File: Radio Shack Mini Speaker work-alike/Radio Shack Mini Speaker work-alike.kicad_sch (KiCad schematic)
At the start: 22 parts, among them J1 SJ1-3525N, J2 SJ1-3525N, Q1 2SC1815, SW1 SW_SPDT, U1 LM386

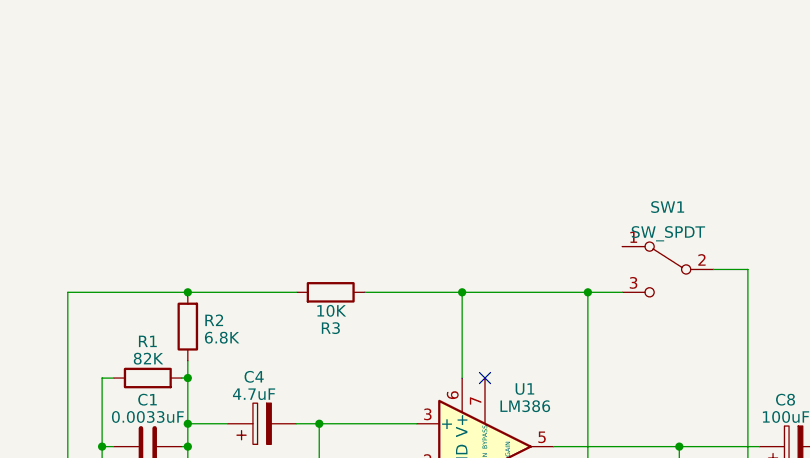
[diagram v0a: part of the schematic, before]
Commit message: added power led
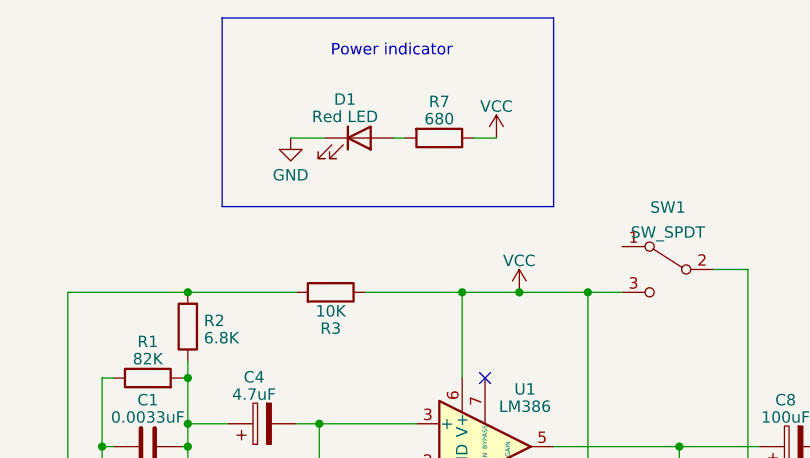
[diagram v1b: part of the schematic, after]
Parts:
- added D1: Red LED, symbol Device:LED
- added R7: 680, symbol Device:R
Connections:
- net GND: now also D1.1 (K)
- net VCC: now reaches C7.1, R3.1, SW1.3 (C), U1.6 (V+)
- net VCC: now also R7.1
- new net: D1.2 (A), R7.2
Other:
- note added: "Power indicator"
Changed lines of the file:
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@@
   (junction (at 125.095 80.645) (diameter 0) (color 0 0 0 0)
+  )
+  (junction (at 131.445 80.645) (diameter 0) (color 0 0 0 0)
   )
   (junction (at 109.22 95.25) (diameter 0) (color 0 0 0 0)
@@
     (stroke (width 0) (type default))
   )
+  (wire (pts (xy 126.365 63.5) (xy 128.905 63.5))
+    (stroke (width 0) (type default))
+  )
   (wire (pts (xy 139.065 80.645) (xy 139.065 109.22))
     (stroke (width 0) (type default))
@@
     (stroke (width 0) (type default))
   )
-  (wire (pts (xy 125.095 80.645) (xy 139.065 80.645))
+  (wire (pts (xy 125.095 80.645) (xy 131.445 80.645))
     (stroke (width 0) (type default))
   )
@@
     (stroke (width 0) (type default))
   )
+  (wire (pts (xy 106.045 63.5) (xy 109.855 63.5))
+    (stroke (width 0) (type default))
+  )
   (wire (pts (xy 109.22 124.46) (xy 109.22 121.92))
     (stroke (width 0) (type default))
@@
     (stroke (width 0) (type default))
   )
+  (wire (pts (xy 131.445 80.645) (xy 139.065 80.645))
+    (stroke (width 0) (type default))
+  )
   (wire (pts (xy 149.225 113.665) (xy 149.225 108.585))
     (stroke (width 0) (type default))
@@
     (stroke (width 0) (type default))
   )
+  (wire (pts (xy 117.475 63.5) (xy 118.745 63.5))
+    (stroke (width 0) (type default))
+  )
   (wire (pts (xy 174.625 113.665) (xy 169.545 113.665))
     (stroke (width 0) (type default))
@@
   (wire (pts (xy 85.09 106.045) (xy 86.995 106.045))
     (stroke (width 0) (type default))
+  )
+  (rectangle (start 98.425 50.165) (end 135.255 71.12)
+    (stroke (width 0) (type default))
+    (fill (type none))
+  )
+  (text "Power indicator" (at 110.49 54.61 0)
+    (effects (font (size 1.27 1.27)) (justify left bottom))
   )
   (symbol (lib_id "Device:C_Polarized") (at 131.445 111.76 90) (unit 1)
@@
     )
   )
+  (symbol (lib_id "power:VCC") (at 131.445 80.645 0) (unit 1)
+    (in_bom yes) (on_board yes) (dnp no) (fields_autoplaced)
+    (property "Reference" "#PWR01" (at 131.445 84.455 0)
+      (effects (font (size 1.27 1.27)) hide)
+    )
+    (property "Value" "VCC" (at 131.445 77.1431 0)
+      (effects (font (size 1.27 1.27)))
+    )
+    (property "Footprint" "" (at 131.445 80.645 0)
+      (effects (font (size 1.27 1.27)) hide)
+    )
+    (property "Datasheet" "" (at 131.445 80.645 0)
+      (effects (font (size 1.27 1.27)) hide)
+    )
+    (pin "1")
+    (instances
+      (project "Radio Shack Mini Speaker work-alike"
+        (path "/107d545c-a928-4c25-a52f-96fe59686438"
+          (reference "#PWR01") (unit 1)
+        )
+      )
+    )
+  )
   (symbol (lib_id "Evan's misc parts:SJ1-3525N") (at 41.91 102.87 0) (mirror x) (unit 1)
     (in_bom yes) (on_board yes) (dnp no) (fields_autoplaced)
@@
     )
   )
+  (symbol (lib_id "power:VCC") (at 128.905 63.5 0) (unit 1)
+    (in_bom yes) (on_board yes) (dnp no) (fields_autoplaced)
+    (property "Reference" "#PWR04" (at 128.905 67.31 0)
+      (effects (font (size 1.27 1.27)) hide)
+    )
+    (property "Value" "VCC" (at 128.905 59.9981 0)
+      (effects (font (size 1.27 1.27)))
+    )
+    (property "Footprint" "" (at 128.905 63.5 0)
+      (effects (font (size 1.27 1.27)) hide)
+    )
+    (property "Datasheet" "" (at 128.905 63.5 0)
+      (effects (font (size 1.27 1.27)) hide)
+    )
+    (pin "1")
+    (instances
+      (project "Radio Shack Mini Speaker work-alike"
+        (path "/107d545c-a928-4c25-a52f-96fe59686438"
+          (reference "#PWR04") (unit 1)
+        )
+      )
+    )
+  )
+  (symbol (lib_id "Device:LED") (at 113.665 63.5 0) (unit 1)
+    (in_bom yes) (on_board yes) (dnp no) (fields_autoplaced)
+    (property "Reference" "D1" (at 112.0775 59.2201 0)
+      (effects (font (size 1.27 1.27)))
+    )
+    (property "Value" "Red LED" (at 112.0775 61.1411 0)
+      (effects (font (size 1.27 1.27)))
+    )
+    (property "Footprint" "" (at 113.665 63.5 0)
+      (effects (font (size 1.27 1.27)) hide)
+    )
+    (property "Datasheet" "~" (at 113.665 63.5 0)
+      (effects (font (size 1.27 1.27)) hide)
+    )
+    (pin "1")
+    (pin "2")
+    (instances
+      (project "Radio Shack Mini Speaker work-alike"
+        (path "/107d545c-a928-4c25-a52f-96fe59686438"
+          (reference "D1") (unit 1)
+        )
+      )
+    )
+  )
   (symbol (lib_id "Device:R_Potentiometer") (at 67.31 106.045 0) (unit 1)
     (in_bom yes) (on_board yes) (dnp no) (fields_autoplaced)
@@
         )
       )
+    )
+  )
+  (symbol (lib_id "Device:R") (at 122.555 63.5 270) (unit 1)
+    (in_bom yes) (on_board yes) (dnp no)
+    (property "Reference" "R7" (at 122.555 59.4741 90)
+      (effects (font (size 1.27 1.27)))
+    )
+    (property "Value" "680" (at 122.555 61.3951 90)
+      (effects (font (size 1.27 1.27)))
+    )
+    (property "Footprint" "" (at 122.555 61.722 90)
+      (effects (font (size 1.27 1.27)) hide)
+    )
+    (property "Datasheet" "~" (at 122.555 63.5 0)
+      (effects (font (size 1.27 1.27)) hide)
+    )
+    (pin "1")
+    (pin "2")
+    (instances
+      (project "Radio Shack Mini Speaker work-alike"
+        (path "/107d545c-a928-4c25-a52f-96fe59686438"
+          (reference "R7") (unit 1)
+        )
+      )
+    )
+  )
+  (symbol (lib_id "power:GND") (at 106.045 63.5 0) (unit 1)
+    (in_bom yes) (on_board yes) (dnp no) (fields_autoplaced)
+    (property "Reference" "#PWR02" (at 106.045 69.85 0)
+      (effects (font (size 1.27 1.27)) hide)
+    )
+    (property "Value" "GND" (at 106.045 67.6355 0)
+      (effects (font (size 1.27 1.27)))
+    )
+    (property "Footprint" "" (at 106.045 63.5 0)
+      (effects (font (size 1.27 1.27)) hide)
+    )
+    (property "Datasheet" "" (at 106.045 63.5 0)
+      (effects (font (size 1.27 1.27)) hide)
+    )
+    (pin "1")
+    (instances
+      (project "Radio Shack Mini Speaker work-alike"
+        (path "/107d545c-a928-4c25-a52f-96fe59686438"
+          (reference "#PWR02") (unit 1)
+        )
+      )

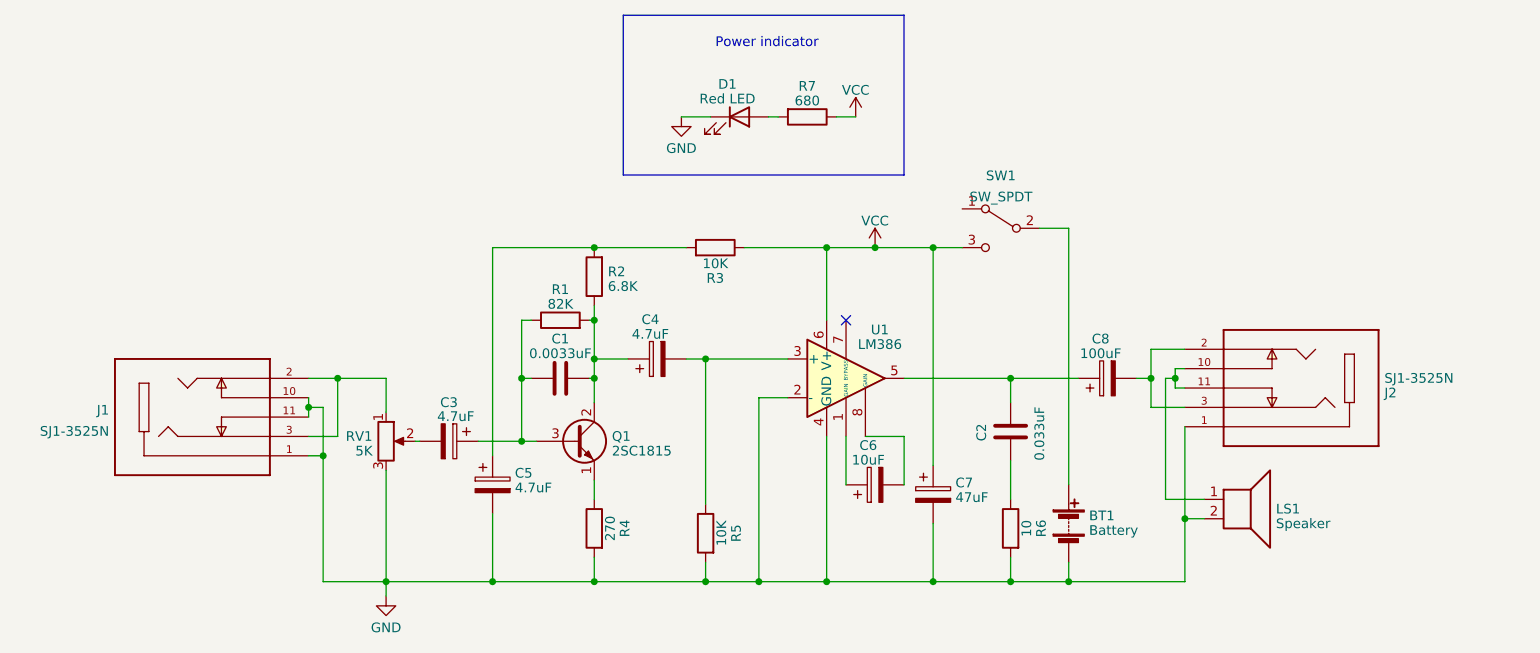
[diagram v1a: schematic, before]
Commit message: tweaked radio shack speaker
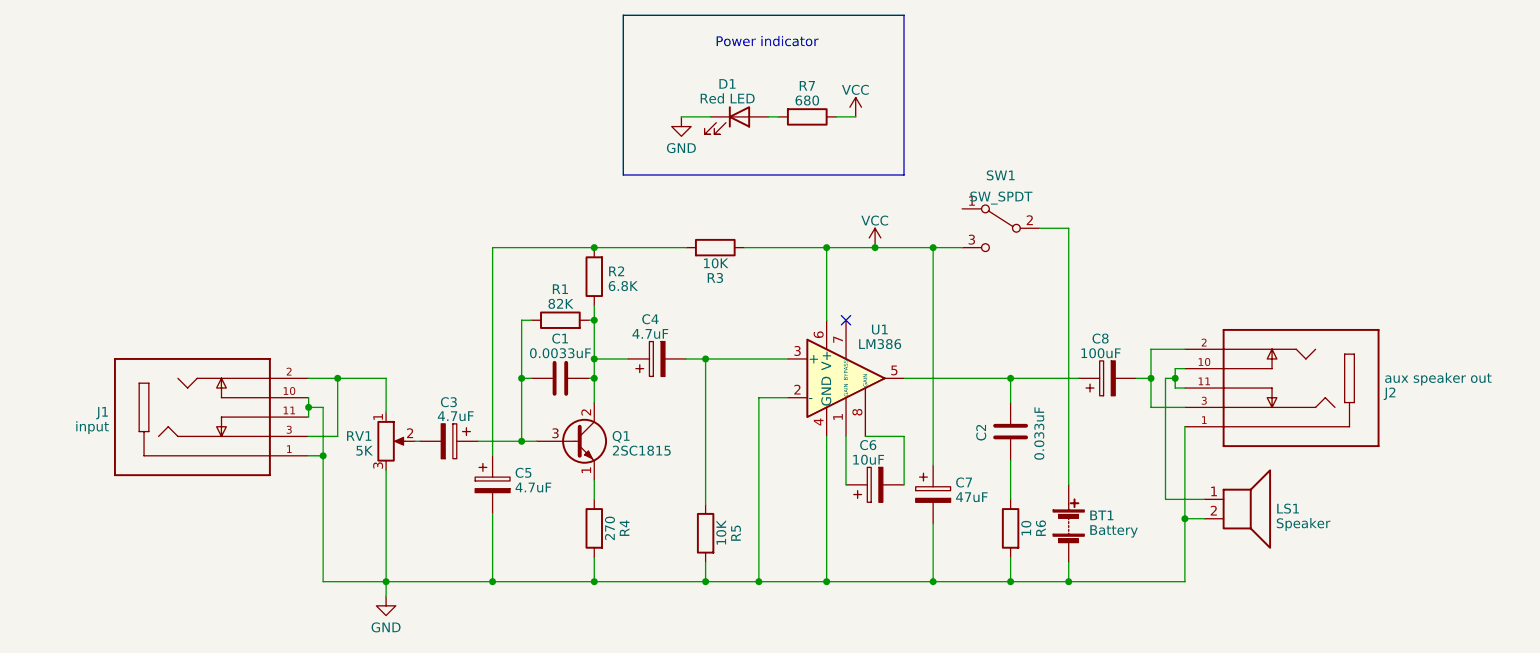
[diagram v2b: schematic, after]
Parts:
- BT1, LS1: footprint (none) -> Connector_PinHeader_2.54mm:PinHeader_1x02_P2.54mm_Vertical
- C6: footprint (none) -> Capacitor_THT:CP_Radial_D5.0mm_P2.50mm
- D1: footprint (none) -> LED_THT:LED_D3.0mm
- J1: value SJ1-3525N -> input; footprint Evan's misc parts:CUI_SJ1-3525N -> Evan's parts:CUI_SJ1-3525N
- J2: value SJ1-3525N -> aux speaker out; footprint Evan's misc parts:CUI_SJ1-3525N -> Evan's parts:CUI_SJ1-3525N
- R1, R2, R3, R4, R5, R6, R7: footprint (none) -> Resistor_THT:R_Axial_DIN0207_L6.3mm_D2.5mm_P10.16mm_Horizontal
- U1: footprint (none) -> Package_DIP:DIP-8_W7.62mm
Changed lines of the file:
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@@
       (effects (font (size 1.27 1.27)))
     )
-    (property "Footprint" "" (at 135.255 110.7948 0)
+    (property "Footprint" "Capacitor_THT:CP_Radial_D5.0mm_P2.50mm" (at 135.255 110.7948 0)
       (effects (font (size 1.27 1.27)) hide)
     )
@@
       (effects (font (size 1.27 1.27)))
     )
-    (property "Footprint" "" (at 151.003 117.475 90)
+    (property "Footprint" "Resistor_THT:R_Axial_DIN0207_L6.3mm_D2.5mm_P10.16mm_Horizontal" (at 151.003 117.475 90)
       (effects (font (size 1.27 1.27)) hide)
     )
@@
       (effects (font (size 1.27 1.27)))
     )
-    (property "Footprint" "" (at 96.393 117.475 90)
+    (property "Footprint" "Resistor_THT:R_Axial_DIN0207_L6.3mm_D2.5mm_P10.16mm_Horizontal" (at 96.393 117.475 90)
       (effects (font (size 1.27 1.27)) hide)
     )
@@
   (symbol (lib_id "Evan's misc parts:SJ1-3525N") (at 41.91 102.87 0) (mirror x) (unit 1)
     (in_bom yes) (on_board yes) (dnp no) (fields_autoplaced)
-    (property "Reference" "J1" (at 30.988 101.9615 0)
-      (effects (font (size 1.27 1.27)) (justify right))
-    )
-    (property "Value" "SJ1-3525N" (at 30.988 104.7366 0)
-      (effects (font (size 1.27 1.27)) (justify right))
-    )
-    (property "Footprint" "Evan's misc parts:CUI_SJ1-3525N" (at 41.91 102.87 0)
+    (property "Reference" "J1" (at 30.9881 102.2263 0)
+      (effects (font (size 1.27 1.27)) (justify right))
+    )
+    (property "Value" "input" (at 30.9881 104.1473 0)
+      (effects (font (size 1.27 1.27)) (justify right))
+    )
+    (property "Footprint" "Evan's parts:CUI_SJ1-3525N" (at 41.91 102.87 0)
       (effects (font (size 1.27 1.27)) (justify left bottom) hide)
     )
@@
       (effects (font (size 1.27 1.27)))
     )
-    (property "Footprint" "" (at 113.665 63.5 0)
+    (property "Footprint" "LED_THT:LED_D3.0mm" (at 113.665 63.5 0)
       (effects (font (size 1.27 1.27)) hide)
     )
@@
       (effects (font (size 1.27 1.27)) (justify left))
     )
-    (property "Footprint" "" (at 179.705 118.745 0)
+    (property "Footprint" "Connector_PinHeader_2.54mm:PinHeader_1x02_P2.54mm_Vertical" (at 179.705 118.745 0)
       (effects (font (size 1.27 1.27)) hide)
     )
@@
       (effects (font (size 1.27 1.27)) (justify right))
     )
-    (property "Footprint" "" (at 96.393 84.455 90)
+    (property "Footprint" "Resistor_THT:R_Axial_DIN0207_L6.3mm_D2.5mm_P10.16mm_Horizontal" (at 96.393 84.455 90)
       (effects (font (size 1.27 1.27)) hide)
     )
@@
       (effects (font (size 1.27 1.27)) (justify left))
     )
-    (property "Footprint" "" (at 156.845 115.316 90)
+    (property "Footprint" "Connector_PinHeader_2.54mm:PinHeader_1x02_P2.54mm_Vertical" (at 156.845 115.316 90)
       (effects (font (size 1.27 1.27)) hide)
     )
@@
       (effects (font (size 1.27 1.27)))
     )
-    (property "Footprint" "" (at 122.555 61.722 90)
+    (property "Footprint" "Resistor_THT:R_Axial_DIN0207_L6.3mm_D2.5mm_P10.16mm_Horizontal" (at 122.555 61.722 90)
       (effects (font (size 1.27 1.27)) hide)
     )
@@
       (effects (font (size 1.27 1.27)))
     )
-    (property "Footprint" "" (at 130.175 95.25 0)
+    (property "Footprint" "Package_DIP:DIP-8_W7.62mm" (at 130.175 95.25 0)
       (effects (font (size 1.27 1.27)) hide)
     )
@@
       (effects (font (size 1.27 1.27)))
     )
-    (property "Footprint" "" (at 110.49 82.423 90)
+    (property "Footprint" "Resistor_THT:R_Axial_DIN0207_L6.3mm_D2.5mm_P10.16mm_Horizontal" (at 110.49 82.423 90)
       (effects (font (size 1.27 1.27)) hide)
     )
@@
       (effects (font (size 1.27 1.27)) (justify right))
     )
-    (property "Value" "SJ1-3525N" (at 198.247 97.7827 0)
-      (effects (font (size 1.27 1.27)) (justify right))
-    )
-    (property "Footprint" "Evan's misc parts:CUI_SJ1-3525N" (at 187.325 99.06 0)
+    (property "Value" "aux speaker out" (at 198.247 97.7827 0)
+      (effects (font (size 1.27 1.27)) (justify right))
+    )
+    (property "Footprint" "Evan's parts:CUI_SJ1-3525N" (at 187.325 99.06 0)
       (effects (font (size 1.27 1.27)) (justify left bottom) hide)
     )
@@
       (effects (font (size 1.27 1.27)))
     )
-    (property "Footprint" "" (at 110.998 118.11 90)
+    (property "Footprint" "Resistor_THT:R_Axial_DIN0207_L6.3mm_D2.5mm_P10.16mm_Horizontal" (at 110.998 118.11 90)
       (effects (font (size 1.27 1.27)) hide)
     )
@@
       (effects (font (size 1.27 1.27)))
     )
-    (property "Footprint" "" (at 90.17 91.948 90)
-      (effects (font (size 1.27 1.27)) hide)
-    )
+    (property "Footprint" "Resistor_THT:R_Axial_DIN0207_L6.3mm_D2.5mm_P10.16mm_Horizontal" (at 90.17 91.948 90)
+      (effects (font (size 1.27 1.27)) hide)
+    )

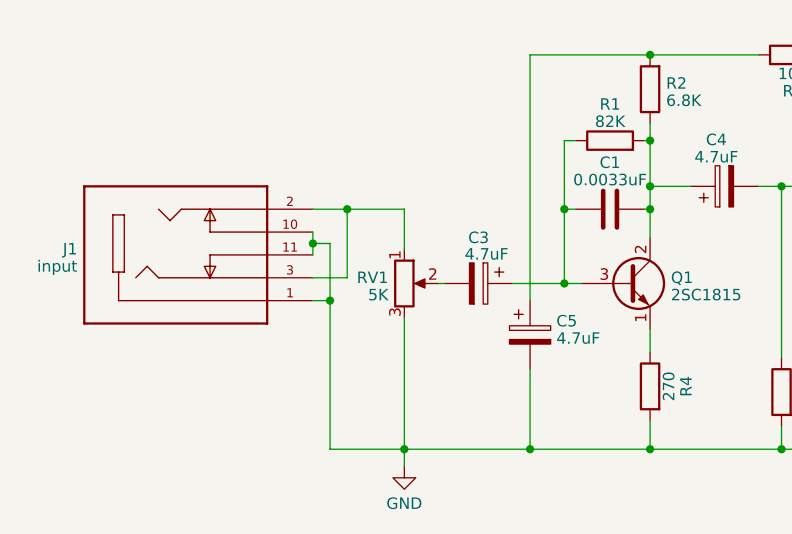
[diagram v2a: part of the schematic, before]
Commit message: updated switch position
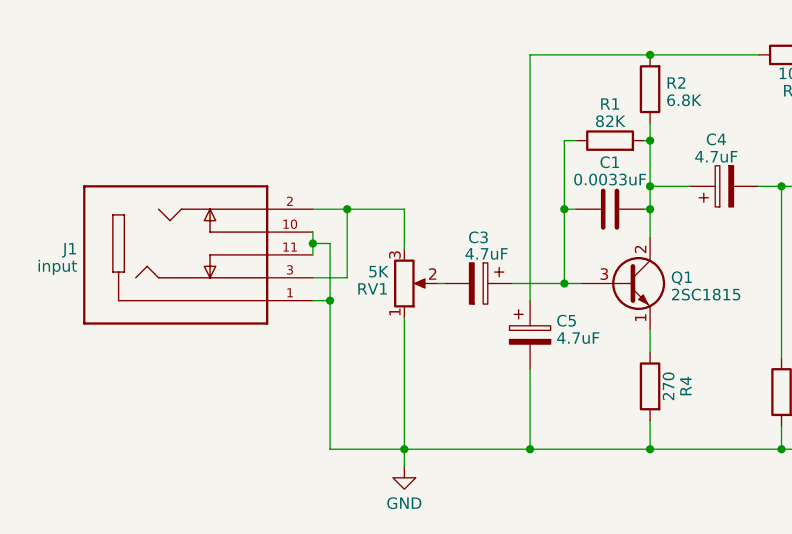
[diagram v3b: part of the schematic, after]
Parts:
- C1: footprint (none) -> Capacitor_THT:C_Disc_D5.0mm_W2.5mm_P2.50mm
- C2: footprint (none) -> Capacitor_THT:C_Disc_D5.0mm_W2.5mm_P5.00mm
- C3, C4, C5, C7: footprint (none) -> Capacitor_THT:CP_Radial_D5.0mm_P2.50mm
- C8: footprint (none) -> Capacitor_THT:CP_Radial_D6.3mm_P2.50mm
- RV1: footprint (none) -> Evan's parts:allen bradlet thumbwheel pot
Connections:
- net GND: now also RV1.1; no longer RV1.3
- net at J1.2, J1.3: now also RV1.3; no longer RV1.1
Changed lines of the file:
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@@
       (effects (font (size 1.27 1.27)) (justify left))
     )
-    (property "Footprint" "" (at 82.2452 115.57 0)
+    (property "Footprint" "Capacitor_THT:CP_Radial_D5.0mm_P2.50mm" (at 82.2452 115.57 0)
       (effects (font (size 1.27 1.27)) hide)
     )
@@
     )
   )
-  (symbol (lib_id "Device:R_Potentiometer") (at 67.31 106.045 0) (unit 1)
-    (in_bom yes) (on_board yes) (dnp no) (fields_autoplaced)
-    (property "Reference" "RV1" (at 65.5321 105.4013 0)
-      (effects (font (size 1.27 1.27)) (justify right))
-    )
-    (property "Value" "5K" (at 65.5321 107.3223 0)
-      (effects (font (size 1.27 1.27)) (justify right))
-    )
-    (property "Footprint" "" (at 67.31 106.045 0)
+  (symbol (lib_id "Device:R_Potentiometer") (at 67.31 106.045 0) (mirror x) (unit 1)
+    (in_bom yes) (on_board yes) (dnp no)
+    (property "Reference" "RV1" (at 65.5321 106.6887 0)
+      (effects (font (size 1.27 1.27)) (justify right))
+    )
+    (property "Value" "5K" (at 65.5321 104.7677 0)
+      (effects (font (size 1.27 1.27)) (justify right))
+    )
+    (property "Footprint" "Evan's parts:allen bradlet thumbwheel pot" (at 67.31 106.045 0)
       (effects (font (size 1.27 1.27)) hide)
     )
@@
       (effects (font (size 1.27 1.27)) (justify left))
     )
-    (property "Footprint" "" (at 150.1902 108.585 0)
+    (property "Footprint" "Capacitor_THT:C_Disc_D5.0mm_W2.5mm_P5.00mm" (at 150.1902 108.585 0)
       (effects (font (size 1.27 1.27)) hide)
     )
@@
       (effects (font (size 1.27 1.27)))
     )
-    (property "Footprint" "" (at 165.735 96.8248 0)
+    (property "Footprint" "Capacitor_THT:CP_Radial_D6.3mm_P2.50mm" (at 165.735 96.8248 0)
       (effects (font (size 1.27 1.27)) hide)
     )
@@
       (effects (font (size 1.27 1.27)) (justify left))
     )
-    (property "Footprint" "" (at 140.0302 116.84 0)
+    (property "Footprint" "Capacitor_THT:CP_Radial_D5.0mm_P2.50mm" (at 140.0302 116.84 0)
       (effects (font (size 1.27 1.27)) hide)
     )
@@
       (effects (font (size 1.27 1.27)))
     )
-    (property "Footprint" "" (at 93.98 96.8248 0)
+    (property "Footprint" "Capacitor_THT:C_Disc_D5.0mm_W2.5mm_P2.50mm" (at 93.98 96.8248 0)
       (effects (font (size 1.27 1.27)) hide)
     )
@@
       (effects (font (size 1.27 1.27)))
     )
-    (property "Footprint" "" (at 71.755 107.0102 0)
+    (property "Footprint" "Capacitor_THT:CP_Radial_D5.0mm_P2.50mm" (at 71.755 107.0102 0)
       (effects (font (size 1.27 1.27)) hide)
     )
@@
       (effects (font (size 1.27 1.27)))
     )
-    (property "Footprint" "" (at 106.68 94.2848 0)
-      (effects (font (size 1.27 1.27)) hide)
-    )
+    (property "Footprint" "Capacitor_THT:CP_Radial_D5.0mm_P2.50mm" (at 106.68 94.2848 0)
+      (effects (font (size 1.27 1.27)) hide)
+    )
